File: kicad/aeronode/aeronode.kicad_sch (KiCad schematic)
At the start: 48 parts, among them J1 IMU_BOARD, J2 USB-C PD / recovery, J3 2S LiFePO4 6Ah + BMS, Q1 NMOS pass - TBD, U1 ConnectCore93_LGA, U2 CYPD3177-24LQ, U3 BQ25798, U4 LMR33630ADDA, U5 LTC4364CMS

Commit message: [LIMA] aeronode: add BME690 environmental sensor on I2C4; author the symbol
Bosch BME690 (gas / temperature / humidity / pressure, LGA-8 3x3mm) is not in
the KiCad libraries, so the symbol was authored at kicad/lib/Bosch.kicad_sym
from the datasheet's Table 26 rather than assumed compatible with the BME680.

  1,7 GND -> GND      2 CSB -> +3V3      3 SDI -> ENV_SDA
  4 SCK -> ENV_SCL    5 SDO -> GND       6 VDDIO, 8 VDD -> +3V3

On I2C4 (pads E29/F28); I2C3 stays reserved for A2B control. R25/R26 4.7k
pull-ups, C13/C14 100nF on VDD and VDDIO. SDO to GND gives address 0x76.

CSB is hard-wired to +3V3, deliberately not to a GPIO. The datasheet: pulling
CSB down once activates SPI and disables I2C 'until the next power-on-reset',
and if CSB is on a programmable pin that pin must already output VDDIO during
POR or the device locks in SPI mode. A hard wire removes any dependence on GPIO
state at reset. There is an internal 70-190k pull-up as well, but that is not
something to rely on for interface selection.

R25 is not bus convention - SDI is open-drain and the datasheet requires an
external pull-up.

The 8-pin package has no interrupt output, so the sensor is polled. No GPIO was
consumed and U29 remains the last free 3V3 GPIO.

Verified: symbol pins 1-8 match the footprint pads exactly both directions. The
datasheet notes the unusual clockwise-from-top pin numbering, which is why the
ClockwisePinNumbering footprint variant is the correct one. ENV_SDA/ENV_SCL
land on 3 endpoints each. ERC 180, no isolated labels, no pin_to_pin.
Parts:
- added C13, C14: 100nF, symbol Device:C
- added R25, R26: 4.7k, symbol Device:R
- added U6: BME690, Package_LGA:Bosch_LGA-8_3x3mm_P0.8mm_ClockwisePinNumbering, symbol Bosch:BME690
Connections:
- net +3V3: now also C13.1, C14.1, R25.1, R26.1, U6.2 (CSB), U6.6 (VDDIO), U6.8 (VDD)
- net GND: now also C13.2, C14.2, U6.1 (GND), U6.5 (SDO), U6.7 (GND)
- net ENV_SDA: now reaches U1.E29 (I2C4_SDA)
- net ENV_SDA: now also R25.2, U6.3 (SDI)
- net ENV_SCL: now reaches U1.F28 (I2C4_SCL)
- net ENV_SCL: now also R26.2, U6.4 (SCK)

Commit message: [LIMA] aeronode: add u-blox DAN-F10N GNSS on LPUART5; correct the boot-strap list
DAN-F10N L1/L5 dual-band with integrated 20x20x8mm patch antenna. Not in the
KiCad libraries, so the symbol was authored at kicad/lib/ublox.kicad_sym from
the datasheet's Table 11. 56 pins: 36 GND, 7 Reserved, 13 functional.

The module has NO I2C and NO SPI - it is UART only, which drove the allocation:

  TXD 10 -> GNSS_TXD -> AK25 (LPUART5_RX)
  RXD  9 -> GNSS_RXD -> AK24 (LPUART5_TX)
  TIMEPULSE 20 -> GNSS_PPS -> U29
  ANT_CTRL 32 -> GND (internal patch antenna, the default)
  VCC 52/53, V_BCKP 55 -> +3V3; 36 GND on one rail + 34 junctions

LPUART5 was the ONLY free 3.3V UART. LPUART6 is the console; 7 and 8 went to the
IMU SPI buses; 1 and 2 land on Bluetooth pads and boot straps; 3 and 4 are only
reachable on 1V8 ENET pads, and the DAN-F10N's V_PIO is referenced to VCC so
1.8V logic would not meet its input-high threshold. Cost: I2C3 is consumed, so
A2B control now shares I2C4 with the BME690 (no address clash). U29 was the last
free 3V3 GPIO and PPS took it.

HAZARD recorded: SAFEBOOT_N is internally tied to TIMEPULSE through a 1k series
resistor, and the receiver enters safeboot if that pin is low at startup. U29
must therefore be an input/high-Z at reset - if it comes up output-low it will
force safeboot on every power-up.

Also recorded: the datasheet contradicts itself. Table 11 gives RXD=9/TXD=10/
TIMEPULSE=20; Table 12 on the next page gives RXD=21/TXD=20/TIMEPULSE=3 -
numbers that look copied from another module. The symbol follows Table 11, which
is self-consistent with the 56-pin package and the pinout figure. Worth checking
against the integration manual before fab.

CORRECTION to earlier work: the LGA boot-strap list was incomplete. I reported
three (F11, C17, E17); there are four. BOOT_MODE0 is E13. The Design Guidelines
call it BT_UART1_TX while the pad table calls it BT_UART1_TXD, and my exact
string match silently missed it. Nothing in the design touches any strap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
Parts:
- added C15: 10uF, symbol Device:C
- added C16: 100nF, symbol Device:C
- added U7: DAN-F10N, symbol ublox:DAN-F10N
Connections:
- net +3V3: now also C15.1, C16.1, U7.52 (VCC), U7.53 (VCC), U7.55 (V_BCKP)
- net GND: now also C15.2, C16.2, U7.1 (GND), U7.13 (GND), U7.14 (GND), U7.15 (GND), U7.19 (GND), U7.2 (GND), U7.21 (GND), U7.22 (GND), U7.23 (GND), U7.26 (GND), U7.27 (GND), U7.28 (GND), U7.29 (GND), U7.3 (GND), U7.30 (GND), U7.32 (ANT_CTRL), U7.33 (GND), U7.35 (GND), U7.37 (GND), U7.38 (GND), U7.4 (GND), U7.40 (GND), U7.41 (GND), U7.42 (GND), U7.43 (GND), U7.44 (GND), U7.47 (GND), U7.48 (GND), U7.49 (GND), U7.5 (GND), U7.50 (GND), U7.51 (GND), U7.54 (GND), U7.56 (GND), U7.6 (GND), U7.7 (GND), U7.8 (GND)
- net GNSS_RXD: now reaches U1.AK24 (I2C3_SDA)
- net GNSS_RXD: now also U7.9 (RXD)
- net GNSS_TXD: now reaches U1.AK25 (I2C3_SCL)
- net GNSS_TXD: now also U7.10 (TXD)
- net GNSS_PPS: now reaches U1.U29 (CAN1_RX)
- net GNSS_PPS: now also U7.20 (TIMEPULSE)

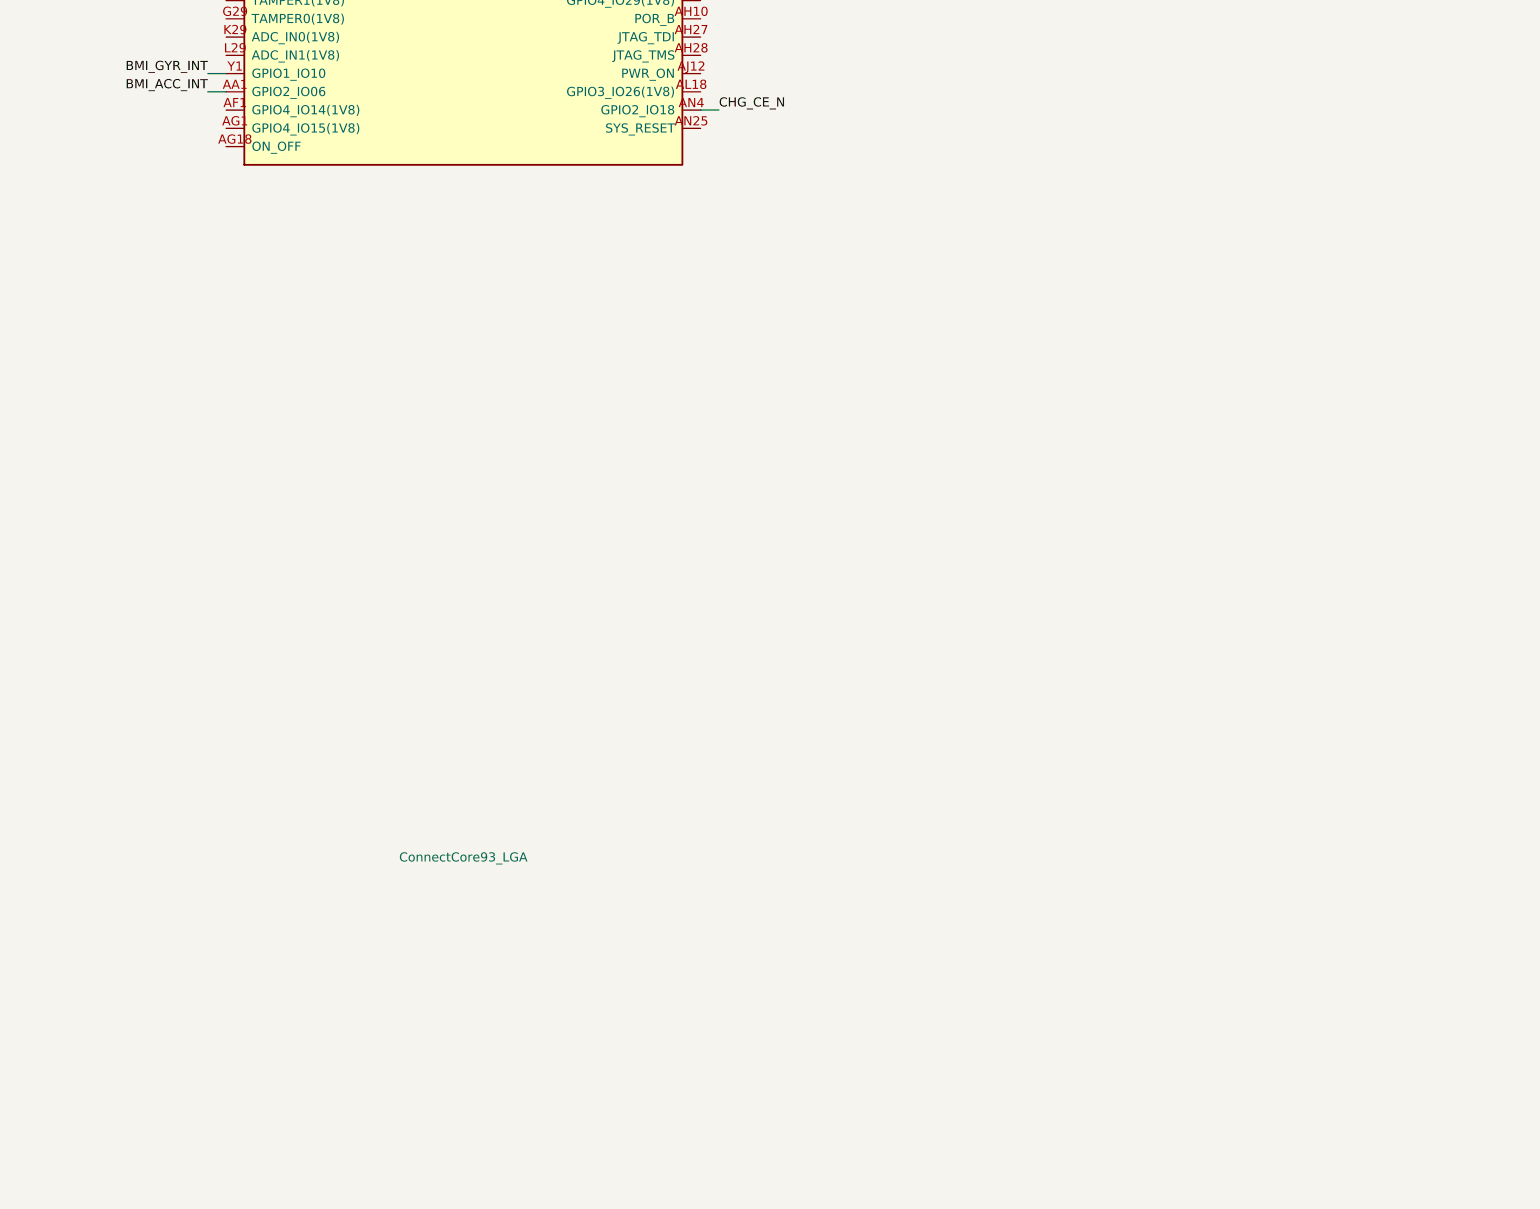
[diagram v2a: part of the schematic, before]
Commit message: [LIMA] aeronode: add SW1 on/off button on ON_OFF (AG18)
Momentary push button from ON_OFF to GND, R27 100R series, C17 100nF debounce.

AG18 is the HRM's 'ON/OFF signal from the CPU (active low)' and the Design
Guidelines confirm it is the module's default power on/off line with an internal
pull-up. The PMIC watches it even when the SOM is off, so one momentary button
gives both power-on and shutdown - a true on/off, not just a wake.

The pin sits on the module's INTERNAL 1.8V supply, which is why the button goes
to GND and nothing pulls it up. An external pull-up to 3V3 would over-drive a
1.8V-referenced input; the internal pull-up already sets the idle state.

PWR_ON (AJ12) deliberately left unconnected - the pad table says 'Output signal.
Do not drive this line externally.' It indicates PMIC state and could drive a
power LED, but it is on an internal supply so it would need a buffer.

Recorded clearly: this is a SOFT off. SW1 shuts down the SOM's PMIC but does not
disconnect the battery - charger, buck and OVP keep drawing. The dominant known
term is the LTC4364 at 370uA typical, plus ~25uA for the LMR33630; the BQ25798
quiescent is not yet quantified. Order-1 mA drains a 6Ah pack over months: fine
for daily use, not fine for storage.

The complement already exists on the part and is left unwired as a decision, not
an oversight: BQ25798 SDRV drives an external ship FET to disconnect the battery,
and QON exits ship mode on a ~1s low. Storage-grade power control would be a
second button on QON plus that ship FET, with software entering ship mode on a
long press.

Verified: ON_OFF_N on 3 endpoints, ON_OFF_SW on 2. ERC 185, down from 187 since
ON_OFF was previously an undriven input.
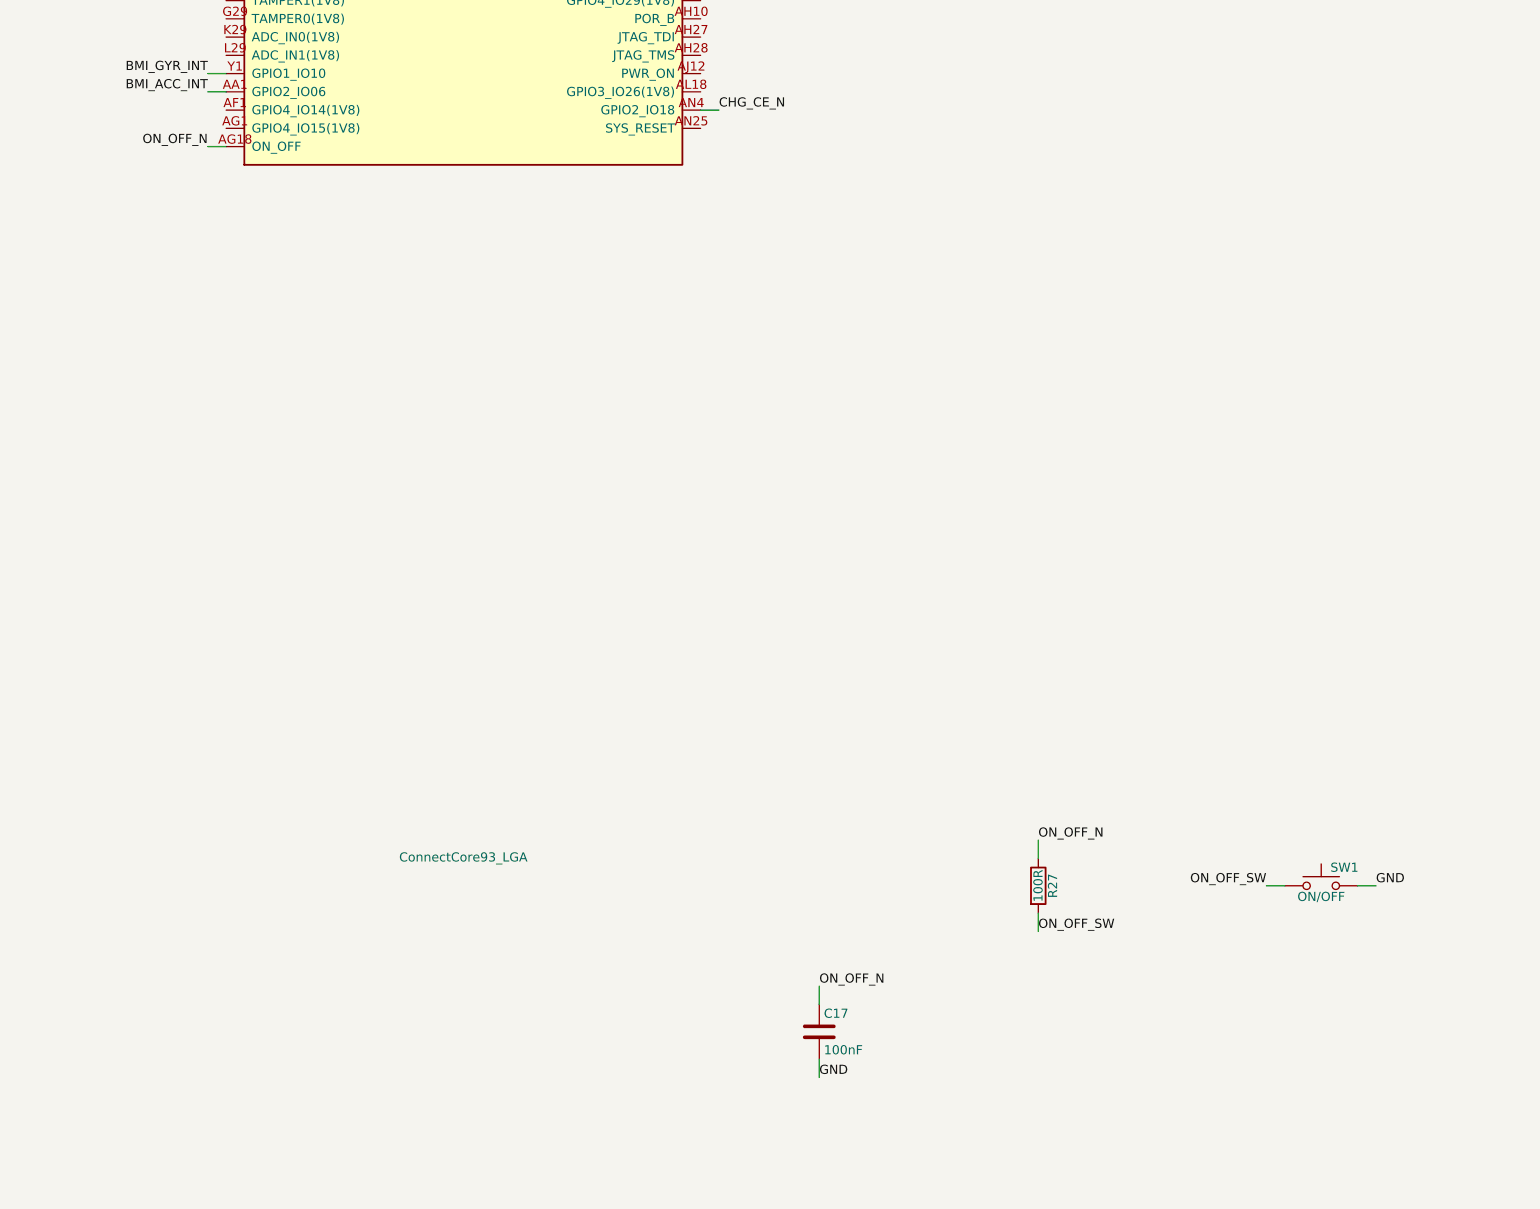
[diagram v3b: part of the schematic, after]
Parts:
- added C17: 100nF, symbol Device:C
- added R27: 100R, symbol Device:R
- added SW1: ON/OFF, symbol Switch:SW_Push
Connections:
- net GND: now also C17.2, SW1.2
- net ON_OFF_N: now reaches U1.AG18 (ON_OFF)
- net ON_OFF_N: now also C17.1, R27.1
- new net ON_OFF_SW: R27.2, SW1.1

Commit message: [LIMA] aeronode: add red/green/blue status LEDs on direct GPIO, no expander
D2 red C18 (GPIO1_IO12) R28 160R, D3 green D18 (GPIO1_IO14) R29 150R,
D4 blue R29 pad (GPIO2_IO27) R30 68R. LEDs sink into the GPIO - anode to +3V3
through the resistor, cathode to the pin - so active low, and the pin sinks
rather than sources.

Finding three pins was the work. There were ZERO free 3V3 GPIO. Every other
GPIO-capable pad is on the 1V8 rail, and 1.8V cannot forward-bias a blue LED at
all; sinking a 3V3 LED into a 1V8 pad would inject current into that rail.

C18/D18 were recovered by re-examining an over-broad exclusion in my earlier
scan: they are SPI1_SIN and SPI1_SOUT, SPI1 is unused here (the IMUs use LPSPI3
and LPSPI8), and neither is a boot strap - only SPI1_CS0 and SPI1_SCK are.

The third came from reallocating PG_5V. That signal said the 5V rail was good,
but if it were not the module reading it would not be running - near tautological
on this topology. Overvoltage, the case that actually matters, is still covered
by OVP_FLT_N. PG_5V survives as U4 pin 4 plus its pull-up, so it stays probeable.

AeroNode now has no spare 3.3V GPIO at all. Anything further needs a 1V8 pad
with a shifter, the SD2 pads at the cost of microSD, or dropping a function.

WARNING recorded on the blue: Vf runs 2.8-3.2V, so on 3.3V the resistor sees
only 0.1-0.5V and current is very sensitive to spread - 5.9mA typical but 1.5mA
at worst-case Vf, a 4x brightness variation. R30 is provisional until a specific
blue LED with Vf max <= 3.0V is chosen.

Verified: all six LED nets land on 2 endpoints each, PG_5V correctly reduced to
2. ERC 183, no isolated labels, no pin_to_pin.
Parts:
- added D2: RED, symbol Device:LED
- added D3: GREEN, symbol Device:LED
- added D4: BLUE, symbol Device:LED
- added R28: 160R, symbol Device:R
- added R29: 150R, symbol Device:R
- added R30: 68R, symbol Device:R
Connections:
- net +3V3: now also R28.1, R29.1, R30.1
- net PG_5V: no longer U1.R29 (CAN2_RX)
- net LED_RED_N: now reaches U1.C18 (SPI1_SIN)
- net LED_RED_N: now also D2.1 (K)
- net LED_GRN_N: now reaches U1.D18 (SPI1_SOUT)
- net LED_GRN_N: now also D3.1 (K)
- new net LED_BLU_N: D4.1 (K), U1.R29 (CAN2_RX)
- new net LED_B_A: D4.2 (A), R30.2
- new net LED_G_A: D3.2 (A), R29.2
- new net LED_R_A: D2.2 (A), R28.2

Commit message: [LIMA] aeronode: add MMC5983MA magnetometer on I2C4; rename ENV_* to I2C4_*
MEMSIC MMC5983MA 3-axis AMR magnetometer, LGA-16. Not in the KiCad libraries so
the symbol was authored at kicad/lib/MEMSIC.kicad_sym from the datasheet's pin
description table.

  1 SCL -> I2C4_SCL      16 SDA -> I2C4_SDA
  4 SPI_CS -> +3V3       (datasheet: 'Tie to VDDIO for I2C Interface')
  10 CAP -> C18 10uF     2/13 VDD,VDDIO -> +3V3    9/11 GND
  15 INT, 5 SPI_SDO left open; NC pins no-connect

I2C address 0x30 fixed, no clash with the BME690 at 0x76. Supply 2.8-3.5V, abs
max 3.6V - our 3V3 sits inside with about 0.23V of margin.

C18 is NOT decoupling. Pin 10 is the energy store for the degaussing coil that
performs SET/RESET offset cancellation - the mechanism by which an AMR sensor
removes its own offset drift. Omit it and SET/RESET does not work, which costs
accuracy over temperature rather than failing outright. C19/C20 are the real
decoupling.

MAGNETIC INTERFERENCE flagged as the actual design constraint. This board has a
1.5MHz buck-boost switching battery-scale currents, a 400kHz 3A buck, up to 3A
of pack current, and LED currents. A magnetometer near those measures the board,
not the Earth, and calibration cannot remove a time-varying field whose duty
cycle follows the load. Recommended in ARCHITECTURE.md that it move to the
imu-board instead, which is already off-board and away from the power stage.
Left on AeroNode as wired, but raised as a decision to take before layout since
moving it later changes two boards.

Also renamed ENV_SDA/ENV_SCL to I2C4_SDA/I2C4_SCL - naming a shared bus after
one device became misleading once the magnetometer joined, with A2B still to come.

Note: an RM3100-CB symbol was started before the part changed and was removed
rather than left as an unused library file.

Verified: both I2C4 nets land on 4 endpoints (CC93, pull-up, BME690, MMC5983MA),
MAG_CAP on 2, zero ENV_* remaining. ERC 185, no isolated labels.
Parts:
- added C18: 10uF, symbol Device:C
- added C19, C20: 100nF, symbol Device:C
- added U9: MMC5983MA, symbol MEMSIC:MMC5983MA
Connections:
- net +3V3: now also C19.1, C20.1, U9.13 (VDDIO), U9.2 (VDD), U9.4 (SPI_CS)
- net GND: now also C18.2, C19.2, C20.2, U9.11 (GND), U9.9 (GND)
- net ENV_SCL renamed I2C4_SCL
- net I2C4_SCL: now also U9.1 (SCL/SPI_SCK)
- net ENV_SDA renamed I2C4_SDA
- net I2C4_SDA: now also U9.16 (SDA/SPI_SDI)
- new net MAG_CAP: C18.1, U9.10 (CAP)

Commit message: [LIMA] aeronode: add BMP390 barometer at 0x77, avoiding the BME690 address clash
Bosch BMP390, LGA-10. Symbol authored into the existing Bosch.kicad_sym from the
datasheet Table 52.

  2 SCK -> I2C4_SCL     4 SDI -> I2C4_SDA
  5 SDO -> BARO_SA0 -> R31 10k -> +3V3   (address bit = 1)
  6 CSB -> +3V3 (selects I2C)
  1/10 VDDIO,VDD -> +3V3;  3/8/9 VSS -> GND;  7 INT left open, polled

ADDRESS CLASH AVOIDED: Bosch pressure sensors default to 0x76, which the BME690
already holds on this bus. SDO tied high puts the BMP390 at 0x77. The datasheet
also warns SDO must not float or the address is undefined, so it is strapped
rather than left open.

I2C4 now carries 0x30 MMC5983MA, 0x76 BME690, 0x77 BMP390. Recorded in
ARCHITECTURE.md as a map to check before anything else joins the bus.

R31 rather than a direct strap because SDO is bidirectional - an output in SPI
mode - so a hard tie to the rail would be a short if the part ever left I2C. ERC
flagged precisely that (pin_to_pin, bidirectional against power output) and the
10k is the correct fix rather than an exclusion, since SDO is high-Z in I2C mode.
Noted that the BME690's SDO is currently a direct tie to GND - same pattern,
benign while CSB holds I2C mode, and could be matched if wanted.

Also recorded the datasheet warning that holding any interface pin high while
VDDIO is off can permanently damage the part. Everything shares +3V3 here so the
rails collapse together, but it rules out powering the bus from a different
domain than the sensors.

Verified: both I2C4 nets land on 5 endpoints, BARO_SA0 on 2. ERC 186, no
pin_to_pin, no isolated labels.
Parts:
- added C21, C22: 100nF, symbol Device:C
- added R31: 10k, symbol Device:R
- added U10: BMP390, symbol Bosch:BMP390
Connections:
- net +3V3: now also C21.1, C22.1, R31.1, U10.1 (VDDIO), U10.10 (VDD), U10.6 (CSB)
- net GND: now also C21.2, C22.2, U10.3 (VSS), U10.8 (VSS), U10.9 (VSS)
- net I2C4_SCL: now also U10.2 (SCK)
- net I2C4_SDA: now also U10.4 (SDI)
- new net BARO_SA0: R31.2, U10.5 (SDO)
